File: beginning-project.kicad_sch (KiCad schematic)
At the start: 15 parts, among them SW1 SW_Push, SW2 SW_Push, SW3 SW_Push, U1 MAX30102, U2 SSD1306, U3 MAX30102

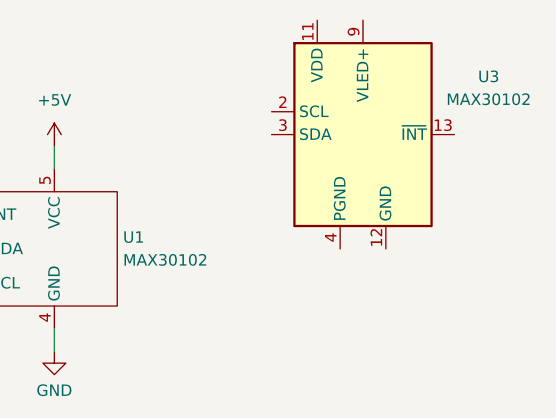
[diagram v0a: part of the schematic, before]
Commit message: chore: remove stock MAX30102 module from schematic
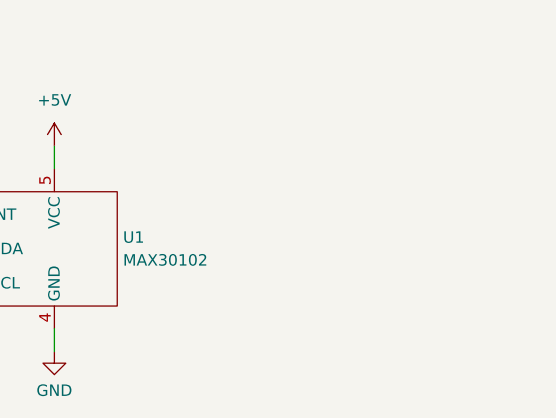
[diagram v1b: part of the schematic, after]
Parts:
- removed U3: MAX30102, OptoDevice:Maxim_OLGA-14_3.3x5.6mm_P0.8mm, symbol Sensor:MAX30102
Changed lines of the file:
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@@
-	)
-	(symbol
-		(lib_id "Sensor:MAX30102")
-		(at 234.95 82.55 0)
-		(unit 1)
-		(body_style 1)
-		(exclude_from_sim no)
-		(in_bom yes)
-		(on_board yes)
-		(in_pos_files yes)
-		(dnp no)
-		(fields_autoplaced yes)
-		(property "Reference" "U3"
-			(at 248.92 76.1298 0)
-			(show_name no)
-			(do_not_autoplace no)
-			(effects
-				(font
-					(size 1.27 1.27)
-				)
-			)
-		)
-		(property "Value" "MAX30102"
-			(at 248.92 78.6698 0)
-			(show_name no)
-			(do_not_autoplace no)
-			(effects
-				(font
-					(size 1.27 1.27)
-				)
-			)
-		)
-		(property "Footprint" "OptoDevice:Maxim_OLGA-14_3.3x5.6mm_P0.8mm"
-			(at 234.95 85.09 0)
-			(hide yes)
-			(show_name no)
-			(do_not_autoplace no)
-			(effects
-				(font
-					(size 1.27 1.27)
-				)
-			)
-		)
-		(property "Datasheet" "https://datasheets.maximintegrated.com/en/ds/MAX30102.pdf"
-			(at 234.95 82.55 0)
-			(hide yes)
-			(show_name no)
-			(do_not_autoplace no)
-			(effects
-				(font
-					(size 1.27 1.27)
-				)
-			)
-		)
-		(property "Description" "Heart Rate Sensor, 14-OLGA"
-			(at 234.95 82.55 0)
-			(hide yes)
-			(show_name no)
-			(do_not_autoplace no)
-			(effects
-				(font
-					(size 1.27 1.27)
-				)
-			)
-		)
-		(pin "6"
-		)
-		(pin "5"
-		)
-		(pin "7"
-		)
-		(pin "9"
-		)
-		(pin "13"
-		)
-		(pin "8"
-		)
-		(pin "4"
-		)
-		(pin "11"
-		)
-		(pin "12"
-		)
-		(pin "3"
-		)
-		(pin "2"
-		)
-		(pin "10"
-		)
-		(pin "1"
-		)
-		(pin "14"
-		)
-		(instances
-			(project "beginning-project"
-				(path "/3573b8f8-7e59-4275-b2bd-ad9bdc983fa4"
-					(reference "U3")
-					(unit 1)
-				)
-			)
-		)
 	)
 	(symbol
